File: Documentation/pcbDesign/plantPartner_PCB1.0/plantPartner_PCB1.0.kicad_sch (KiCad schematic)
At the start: 75 parts, among them IC1 MPM3610, J1 Conn_01x04, J10 Screw_Terminal_01x03, J11 Conn_01x04, J12 Conn_01x03, J13 Conn_01x03, J14 Conn_01x03, J15 Conn_01x03, J16 Conn_01x04, J17 Conn_01x03, J18 Screw_Terminal_01x02, J19 Barrel_Jack, J2 Conn_01x04, J20 Conn_02x04_Top_Bottom, J21 Conn_01x04, J22 Conn_01x04, J23 Conn_01x02, J25 Conn_01x04, J26 Conn_01x01, J27 Conn_01x03, J3 Conn_01x04, J4 Screw_Terminal, J5 Conn_01x02, J6 Screw_Terminal_01x03, J7 Conn_01x03, J8 Conn_02x04_Top_Bottom, J9 Conn_01x03, K1 SRD-05VDC-SL-C, K2 SRD-05VDC-SL-C, Q1 PNP, Q2 PNP, U1 EL357N-G, U2 MAX485, U3 ESP32-DEVKIT-V1, U4 EL357N-G

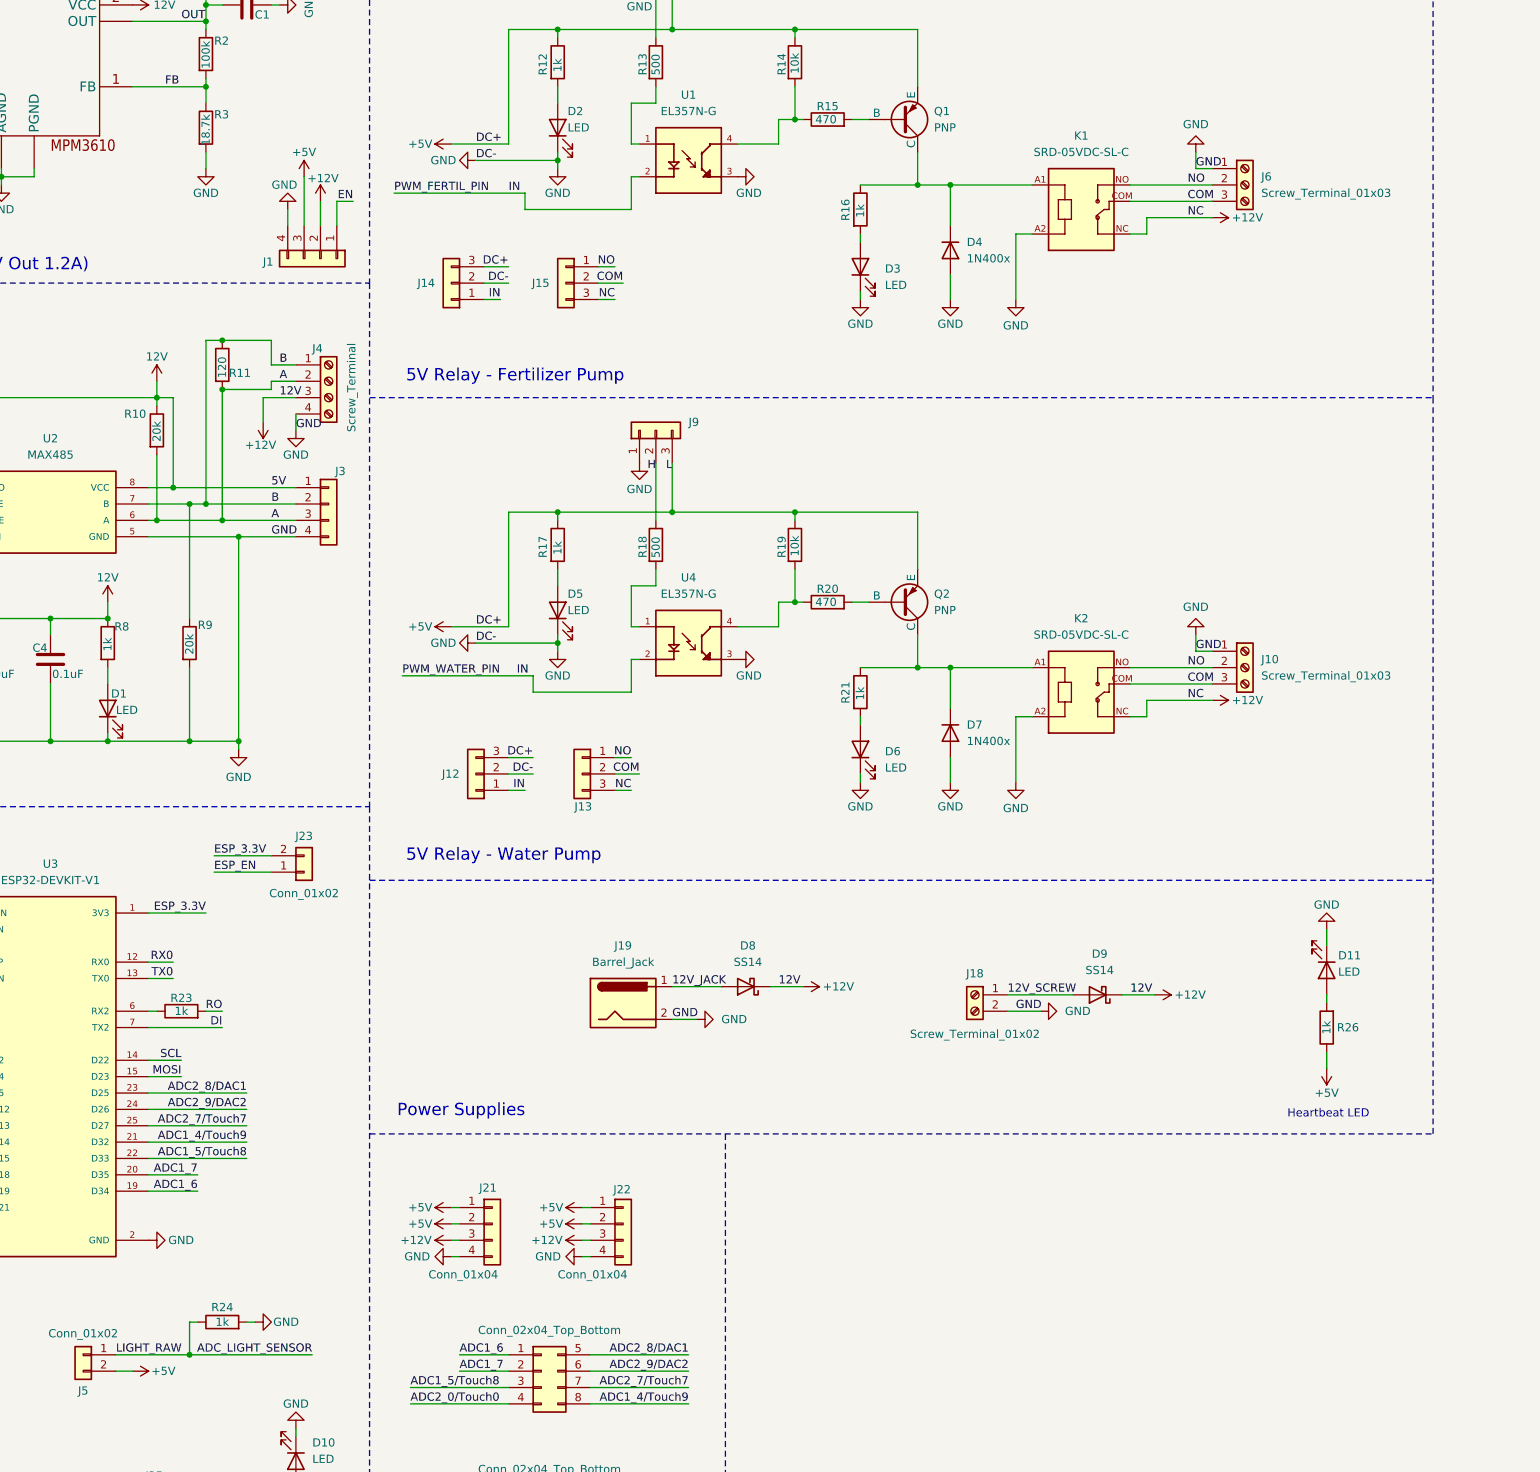
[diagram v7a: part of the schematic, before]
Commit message: Routed the 5V Relays and fixed a schematic issue I made with them. Next is the Buck Converter, RS485 Transceiver, Power Supplies, and ESP32 Signals
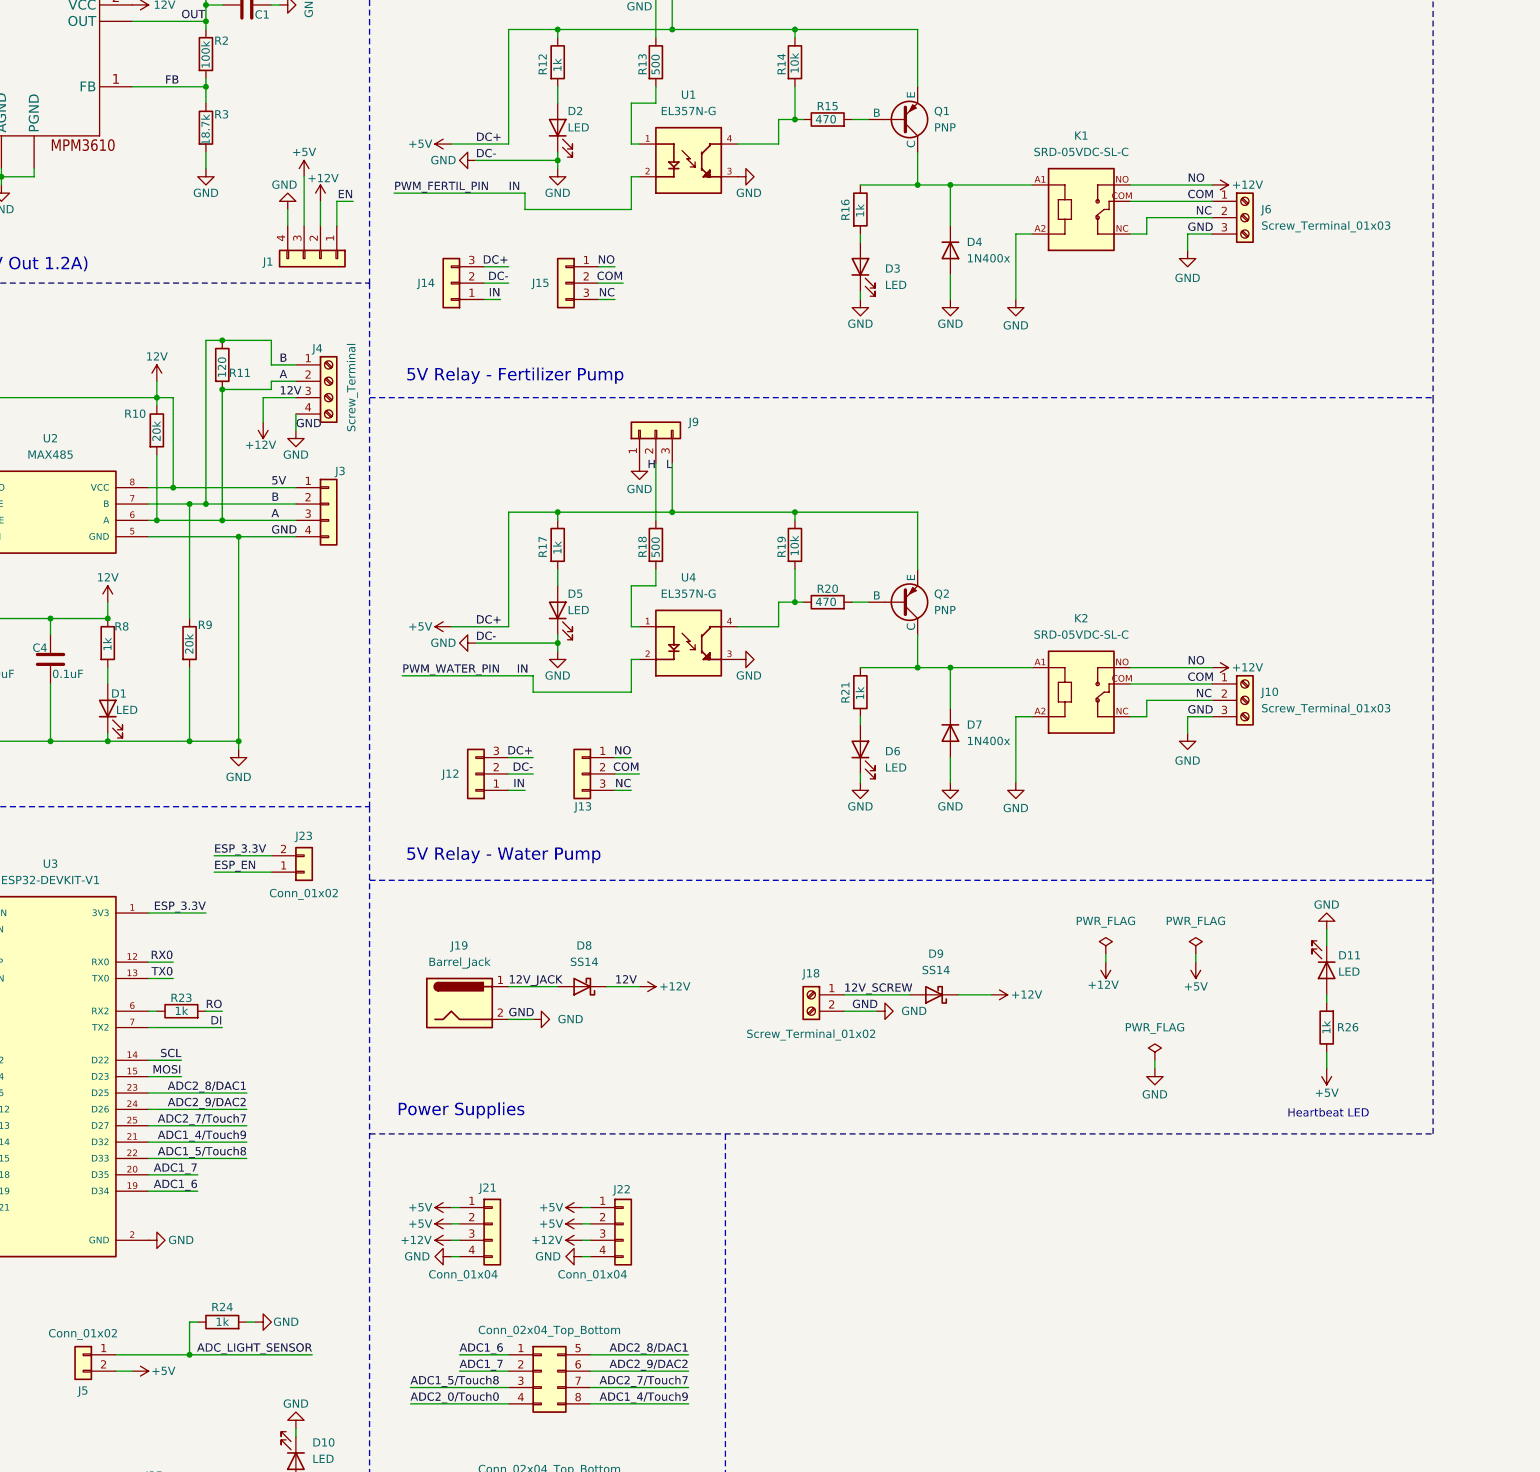
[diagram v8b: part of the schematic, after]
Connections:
- net +12V: now also J13.1 (Pin_1), J15.1 (Pin_1), K1.NO, K2.NO; no longer J13.3 (Pin_3), J15.3 (Pin_3), K1.NC, K2.NC
- net COM: now also J10.1 (Pin_1), J6.1 (Pin_1); no longer J10.3 (Pin_3), J6.3 (Pin_3)
- net GND: now also J10.3 (Pin_3), J6.3 (Pin_3); no longer J10.1 (Pin_1), J6.1 (Pin_1)
- removed net NO: J10.2 (Pin_2), J13.1 (Pin_1), J15.1 (Pin_1), J6.2 (Pin_2), K1.NO, K2.NO
- new net NC: J10.2 (Pin_2), J13.3 (Pin_3), J15.3 (Pin_3), J6.2 (Pin_2), K1.NC, K2.NC
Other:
- moved on the sheet: D8, D9, J18, J19
